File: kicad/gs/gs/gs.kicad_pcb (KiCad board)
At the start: 2 copper layers, 200 x 223.2 mm, 49 parts, among them J1 Jack_12V, J2 JST_MotorAz, J3 JST_MotorEl, J5 Breakout_DIP, J6 JST_ZeroAZ, U1 ESP32-WROOM-32-DEV, U2 MPU-9250-DEV, U3 Ai-Thinker-Ra-02, U4 L7805, U5 LD1117S33TR_SOT223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

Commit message: Finished second revision of GS PCB
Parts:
- added J4: Conn_02x10_Odd_Even, Connector_PinHeader_2.54mm:PinHeader_2x10_P2.54mm_Vertical, F.Cu at (214.1, 171.4)
- added JP1: PowerSelect_3V3, Connector_PinHeader_2.54mm:PinHeader_1x02_P2.54mm_Vertical, F.Cu at (265.7, 152.1)
- added JP2: PowerSelect_5V, Connector_PinHeader_2.54mm:PinHeader_1x02_P2.54mm_Vertical, F.Cu at (264.7, 114.0)
- added JP3: PowerSelect_24V, Connector_PinHeader_2.54mm:PinHeader_1x02_P2.54mm_Vertical, F.Cu at (149.9, 107.4)
- J5: value Breakout_DIP -> PowerBreakout; footprint Connector_PinSocket_2.54mm:PinSocket_1x10_P2.54mm_Vertical -> Connector_PinHeader_2.54mm:PinHeader_1x05_P2.54mm_Vertical
- U3: footprint RF_Module:Ai-Thinker-Ra-01-LoRa -> RA-02-PCB:RA-02-PCB
- moved J6 135.9 mm to (230.1, 222.8), turned to 180 degrees
- moved J3 101.8 mm to (197.6, 103.0)
- moved J5 97.9 mm to (237.2, 107.2), turned to 90 degrees
- moved J2 93.4 mm to (192.0, 97.0), turned to -90 degrees
- moved U9 54.4 mm to (108.0, 143.5), turned to 90 degrees
- moved U2 41.7 mm to (206.6, 167.3), turned to -90 degrees
- moved C6 24.9 mm to (259.5, 196.6), turned to 180 degrees
- moved C2 20.8 mm to (266.2, 110.3), turned to 90 degrees
- moved C21 17.9 mm to (130.5, 147.3)
- moved C4 17.7 mm to (271.8, 141.0), turned to 180 degrees
- moved C5 15.7 mm to (260.9, 191.5), turned to 0 degrees
- moved U5 13.5 mm to (275.3, 145.0), turned to 180 degrees
- moved R10 13.4 mm to (206.2, 64.3), turned to -90 degrees
- moved U4 13.0 mm to (274.8, 117.3), turned to 180 degrees
- moved C19 11.8 mm to (202.4, 66.5), turned to 90 degrees
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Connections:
- net Net-(J2-Pin_1) renamed M1_1A
- net Net-(J2-Pin_2) renamed M1_1B
- net Net-(J2-Pin_3) renamed M1_2A
- net Net-(J2-Pin_4) renamed M1_2B
- net Net-(J3-Pin_1) renamed M2_1A
- net Net-(J3-Pin_2) renamed M2_1B
- net Net-(J3-Pin_3) renamed M2_2A
- net Net-(J3-Pin_4) renamed M2_2B
- C2 pad 1: +5V -> 5V_Int
- C3 pad 1: +3V3 -> 3V3_Int
- J1 pad 3: unconnected-(J1-Pad3) -> GND
- J5 pad 1: BRK_TX -> GND
- J5 pad 2: BRK_RX -> GND
- J5 pad 3: BRK_VP -> +24V
- J5 pad 4: BRK_VN -> +5V
- J5 pad 5: BRK_GPIO25 -> +3V3
- U1 pad 10: AZ_ZERO -> M2_P1
- U1 pad 11: M1_I11 -> M2_I11
- U1 pad 12: M1_I12 -> M2_P2
- U1 pad 13: M1_P2 -> M2_I12
- U1 pad 18: BRK_TX -> M1_I01
- U1 pad 19: BRK_RX -> M1_I02
- U1 pad 2: BRK_VP -> AZ_ZERO
- U1 pad 23: RF_NRESET -> BRK_GPIO5
- U1 pad 26: RF_DIO2 -> BRK_GPIO4
- U1 pad 27: RF_DIO1 -> BRK_GPIO2
- U1 pad 3: BRK_VN -> IMU_INT
- U1 pad 4: IMU_INT -> M1_P1
- U1 pad 5: M1_I01 -> M1_I11
- U1 pad 6: M1_I02 -> M1_I12
- U1 pad 7: M1_P1 -> M1_P2
- U1 pad 8: BRK_GPIO25 -> M2_I01
- U1 pad 9: BRK_GPIO26 -> M2_I02
- U3 pad 10: RF_DIO4 -> RF_NSS
- U3 pad 11: RF_DIO5 -> SPI_MOSI
- U3 pad 12: SPI_SCK -> SPI_MISO
- U3 pad 13: SPI_MISO -> SPI_SCK
- U3 pad 14: SPI_MOSI -> RF_DIO5
- U3 pad 15: RF_NSS -> RF_DIO4
- U4 pad 3: +5V -> 5V_Int
- U5 pad 2: +3V3 -> 3V3_Int
- U7 pad 3: +24V -> 24V_Int
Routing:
- net +5V: track 0.00 -> 400.0 mm, vias 0 -> 1
- net +3V3: track 0.00 -> 280.2 mm
- net M1_I11: track 0.00 -> 271.5 mm, vias 0 -> 2
- net M1_I12: track 0.00 -> 260.3 mm, vias 0 -> 1
- net M1_P1: track 0.00 -> 257.1 mm, vias 0 -> 1
- net M1_P2: track 0.00 -> 257.0 mm, vias 0 -> 1
- net M1_I02: track 0.00 -> 222.4 mm, vias 0 -> 2
- net M1_I01: track 0.00 -> 216.8 mm, vias 0 -> 2
- net M2_I02: track 0.00 -> 212.8 mm, vias 0 -> 2
- net SPI_MOSI: track 0.00 -> 210.4 mm, vias 0 -> 1
- net M2_I12: track 0.00 -> 205.7 mm, vias 0 -> 2
- net M2_P2: track 0.00 -> 205.4 mm, vias 0 -> 2
- net M2_I01: track 0.00 -> 192.3 mm, vias 0 -> 2
- net M2_I11: track 0.00 -> 187.6 mm, vias 0 -> 2
- net M2_P1: track 0.00 -> 184.0 mm, vias 0 -> 2
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- added copper zone on B.Cu, net GND
- added copper zone on F.Cu, net GND
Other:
- board size 200 x 223.2 mm -> 198 x 198 mm
- board text added: "+24V"
- board text added: "+24V frm conv"
- board text added: "+24V to PCB"
- board text added: "+3V3"
- board text added: "+3V3 frm reg"
- board text added: "+3V3 to PCB"
- board text added: "+5V"
- board text added: "+5V frm reg"
- board text added: "+5V to PCB"
- board text added: "GND"
- board text added: "GPIO4"
- board text added: "GPIO5"
- board text added: "MotorAz"
- board text added: "MotorEl"
- board text added: "RF_DIO1"
- board text added: "RF_DIO2"
- board text added: "RF_DIO3"
- board text added: "RF_DIO4"
- board text added: "RF_DIO5"
- board text added: "RF_NRESET"
- board text added: "Zero Sensor"

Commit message: 2nd design of GS PCB
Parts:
- added R15: 10k, Resistor_THT:R_Axial_DIN0207_L6.3mm_D2.5mm_P10.16mm_Horizontal, F.Cu at (295.5, 173.0)
- C14, C15: value 820pF -> 100nF; footprint Capacitor_THT:C_Rect_L4.6mm_W2.0mm_P2.50mm_MKS02_FKP02 -> Capacitor_THT:C_Rect_L7.0mm_W4.5mm_P5.00mm
- C16: value 100nF -> 100uF; footprint Capacitor_THT:C_Rect_L7.0mm_W4.5mm_P5.00mm -> Capacitor_THT:CP_Radial_D5.0mm_P2.00mm
- C17: value 100nF -> 820pF; footprint Capacitor_THT:C_Rect_L7.0mm_W4.5mm_P5.00mm -> Capacitor_THT:C_Rect_L4.6mm_W2.0mm_P2.50mm_MKS02_FKP02
- C20: value 100uF -> 820pF; footprint Capacitor_THT:CP_Radial_D5.0mm_P2.00mm -> Capacitor_THT:C_Rect_L4.6mm_W2.0mm_P2.50mm_MKS02_FKP02
- R12: value 1k -> 1Ω
- R13: value 1Ω -> 1k
- moved R12 163.8 mm to (212.3, 230.1)
- moved C19 160.1 mm to (212.1, 226.3)
- moved C15 147.7 mm to (222.8, 219.8), turned to -90 degrees
- moved R10 146.4 mm to (196.7, 210.4), turned to 90 degrees
- moved C3 142.8 mm to (135.1, 115.1), turned to -135 degrees
- moved U5 142.0 mm to (137.3, 111.8), turned to -45 degrees
- moved C17 139.2 mm to (202.2, 223.8), turned to -90 degrees
- moved C4 134.7 mm to (138.9, 118.9), turned to -135 degrees
- moved U8 131.2 mm to (210.3, 209.8)
- moved R9 129.8 mm to (202.2, 219.7), turned to 0 degrees
- moved C16 127.7 mm to (222.6, 215.4), turned to 0 degrees
- moved C14 127.5 mm to (197.0, 214.4), turned to -90 degrees
- moved R14 125.0 mm to (216.4, 194.3), turned to 0 degrees
- moved R4 121.7 mm to (154.4, 194.0), turned to 90 degrees
- moved R11 119.4 mm to (217.2, 218.2), turned to -90 degrees
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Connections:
- net Net-(U6-SENSE1) renamed /M1_Sense1_In
- net Net-(U6-SENSE2) renamed /M1_Sense2_In
- C14 pad 1: Net-(U8-RC1) -> +5V
- C15 pad 1: GND -> +24V
- C15 pad 2: Net-(U8-RC2) -> GND
- C16 pad 1: +5V -> +24V
- C17 pad 1: +24V -> Net-(U8-RC1)
- C18 pad 2: Net-(U8-COMP_IN1) -> Net-(U8-RC2)
- C19 pad 2: Net-(U8-COMP_IN2) -> Net-(U8-COMP_IN1)
- C20 pad 1: +24V -> GND
- C20 pad 2: GND -> Net-(U8-COMP_IN2)
- C4 pad 1: +5V -> 5V_Int
- J2 pad 1: M1_1A -> M1_1B
- J2 pad 2: M1_1B -> M1_1A
- J2 pad 3: M1_2A -> M1_2B
- J2 pad 4: M1_2B -> M1_2A
- J3 pad 1: M2_1A -> M2_1B
- J3 pad 2: M2_1B -> M2_1A
- J3 pad 3: M2_2A -> M2_2B
- J3 pad 4: M2_2B -> M2_2A
- J4 pad 1: BRK_GPIO2 -> RF_DIO1
- J4 pad 10: RF_DIO3 -> SPI_MISO
- J4 pad 11: SPI_MISO -> unconnected-(J4-Pin_11-Pad11)
- J4 pad 12: RF_DIO2 -> SPI_SCK
- J4 pad 14: RF_DIO1 -> RF_DIO5
- J4 pad 16: RF_NRESET -> RF_DIO4
- J4 pad 18: RF_DIO4 -> unconnected-(J4-Pin_18-Pad18)
- J4 pad 2: unconnected-(J4-Pin_2-Pad2) -> BRK_GPIO14
- J4 pad 20: RF_DIO5 -> unconnected-(J4-Pin_20-Pad20)
- J4 pad 3: BRK_GPIO4 -> RF_DIO3
- J4 pad 4: unconnected-(J4-Pin_4-Pad4) -> BRK_GPIO12
- J4 pad 5: BRK_GPIO5 -> RF_DIO2
- J4 pad 6: unconnected-(J4-Pin_6-Pad6) -> BRK_GPIO13
- J4 pad 7: SPI_SCK -> RF_NRESET
- J4 pad 8: unconnected-(J4-Pin_8-Pad8) -> SPI_MOSI
- J4 pad 9: SPI_MOSI -> unconnected-(J4-Pin_9-Pad9)
- J5 pad 3: +24V -> GND
- R11 pad 1: Net-(U8-SENSE1) -> /M2_Sense1_In
- R12 pad 1: Net-(U8-SENSE2) -> /M2_Sense1_In
- R12 pad 2: Net-(U8-COMP_IN2) -> GND
- R13 pad 1: Net-(U8-SENSE1) -> /M2_Sense2_In
- R13 pad 2: GND -> Net-(U8-COMP_IN2)
- R14 pad 1: Net-(U8-SENSE2) -> /M2_Sense2_In
- U1 pad 1: +5V -> unconnected-(U1-EN-Pad1)
- U1 pad 10: M2_P1 -> RF_NSS
- U1 pad 11: M2_I11 -> BRK_GPIO14
- U1 pad 12: M2_P2 -> BRK_GPIO12
- U1 pad 13: M2_I12 -> BRK_GPIO13
- U1 pad 18: M1_I01 -> M2_I01
- U1 pad 19: M1_I02 -> M2_I11
- U1 pad 20: RF_NSS -> M2_P1
- U1 pad 23: BRK_GPIO5 -> M2_P2
- U1 pad 26: BRK_GPIO4 -> M2_I12
- U1 pad 27: BRK_GPIO2 -> M2_I02
- U1 pad 4: M1_P1 -> M1_I01
- U1 pad 6: M1_I12 -> M1_P1
- U1 pad 8: M2_I01 -> M1_I12
- U1 pad 9: M2_I02 -> M1_I02
- U5 pad 3: +5V -> 5V_Int
- U8 pad 23: Net-(U8-SENSE1) -> /M2_Sense1_In
- U8 pad 3: Net-(U8-SENSE2) -> /M2_Sense2_In
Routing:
- net +5V: track 400.0 -> 142.8 mm, vias 1 -> 0
- net M2_I02: track 212.8 -> 42.3 mm, vias 2 -> 0
- net M2_I12: track 205.7 -> 45.7 mm, vias 2 -> 0
- net M2_P2: track 205.4 -> 51.3 mm, vias 2 -> 0
- net M1_I11: track 271.5 -> 122.2 mm, vias 2 -> 0
- net 5V_Int: track 10.8 -> 159.3 mm
- net M1_I12: track 260.3 -> 118.2 mm, vias 1 -> 0
- net M2_I01: track 192.3 -> 50.6 mm, vias 2 -> 0
- net M2_I11: track 187.6 -> 53.0 mm, vias 2 -> 0
- net M1_P1: track 257.1 -> 122.5 mm, vias 1 -> 0
- net M1_P2: track 257.0 -> 122.7 mm, vias 1 -> 0
- net M2_P1: track 184.0 -> 54.1 mm, vias 2 -> 0
- net MREF: track 166.8 -> 46.4 mm, vias 2 -> 0
- net RF_NSS: track 154.4 -> 45.7 mm
- net M1_I02: track 222.4 -> 114.2 mm, vias 2 -> 0
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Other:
- outline, holes or cut-outs redrawn
- board text removed: "+24V"
- board text removed: "+24V frm conv"
- board text removed: "+24V to PCB"
- board text removed: "+3V3"
- board text removed: "+3V3 frm reg"
- board text removed: "+3V3 to PCB"
- board text removed: "+5V"
- board text removed: "+5V frm reg"
- board text removed: "+5V to PCB"
- board text removed: "GND"
- board text removed: "GPIO4"
- board text removed: "GPIO5"
- board text removed: "MotorAz"
- board text removed: "MotorEl"
- board text removed: "RF_DIO1"
- board text removed: "RF_DIO2"
- board text removed: "RF_DIO3"
- board text removed: "RF_DIO4"
- board text removed: "RF_DIO5"
- board text removed: "RF_NRESET"
- board text removed: "Zero Sensor"

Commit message: Finished core of 2nd design of GS PCB
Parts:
- moved R1 7.64 mm to (189.5, 168.4)
- moved R2 7.62 mm to (194.6, 168.4)
- moved C13 6.90 mm to (169.2, 177.0)
- moved U4 6.68 mm to (164.8, 81.1)
- moved C20 3.61 mm to (212.1, 195.1)
- moved R5 3.05 mm to (174.5, 200.2)
- moved C1 2.54 mm to (174.2, 75.4)
- moved R8 1.93 mm to (172.7, 175.8)
- moved R7 1.83 mm to (173.7, 180.3)
- moved C2 1.02 mm to (164.6, 75.4)
- moved J4 0.51 mm to (295.4, 145.3)
- turned C17 to 0 degrees
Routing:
- net +5V: track 142.8 -> 243.2 mm, vias 0 -> 1
- net MREF: track 46.4 -> 142.4 mm, vias 0 -> 2
- net AZ_ZERO: track 0.00 -> 62.6 mm, vias 0 -> 1
- net Net-(U6-COMP_IN2): track 0.00 -> 21.5 mm
- net IMU_INT: track 100.3 -> 115.9 mm, vias 0 -> 1
- net /M1_Sense2_In: track 0.00 -> 15.1 mm
- net RF_NSS: track 45.7 -> 60.7 mm
- net Net-(U6-RC2): track 0.00 -> 13.1 mm
- net RF_DIO0: track 68.8 -> 81.2 mm
- net +12V: track 114.9 -> 121.5 mm
- net Net-(U8-COMP_IN2): track 12.8 -> 18.1 mm
- net /M1_Sense1_In: track 27.9 -> 22.7 mm
- net GND: track 0.00 -> 5.08 mm
- net 5V_Int: track 159.3 -> 154.2 mm
- net 3V3_Int: track 86.8 -> 91.4 mm
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
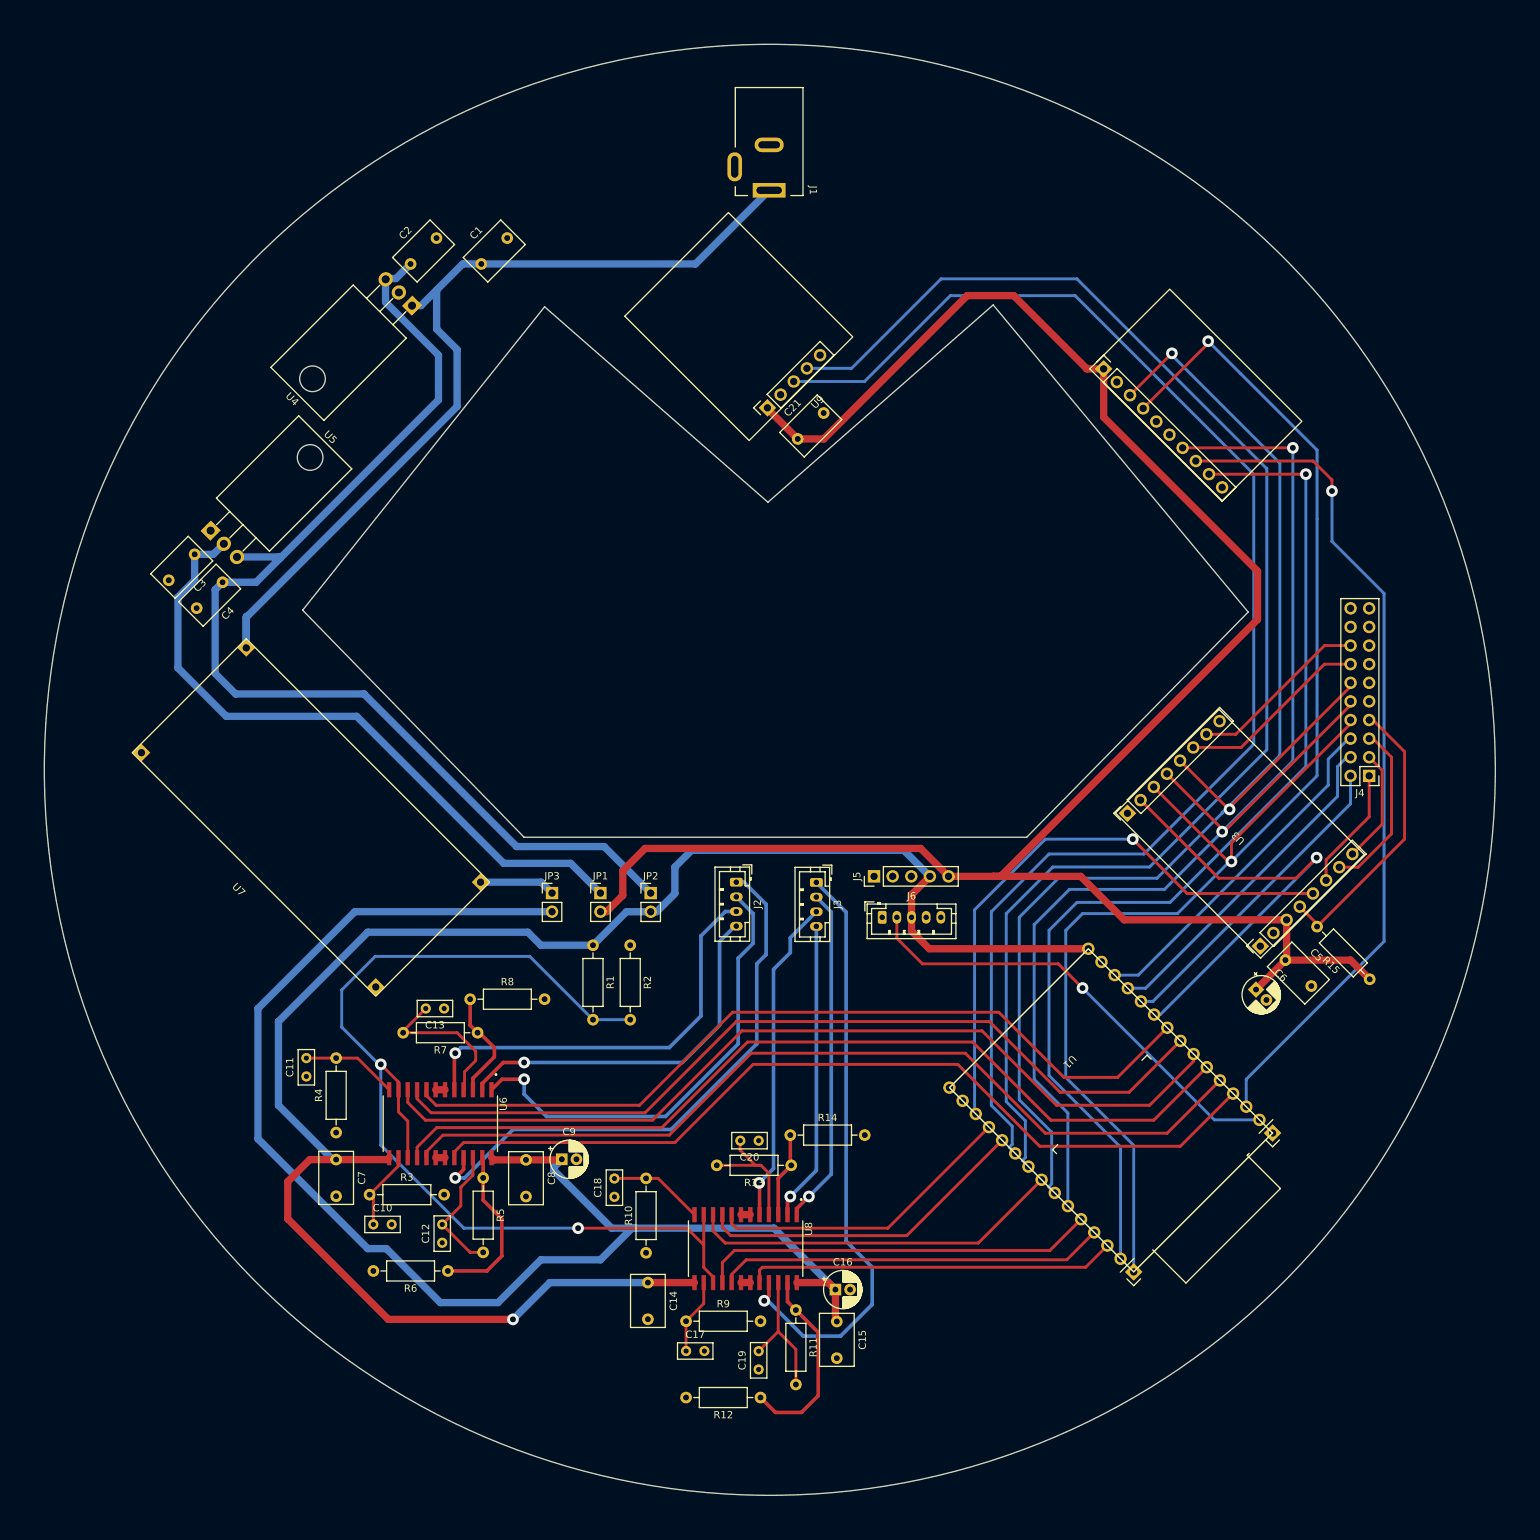
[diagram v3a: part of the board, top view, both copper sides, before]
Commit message: Added details to GS PCB
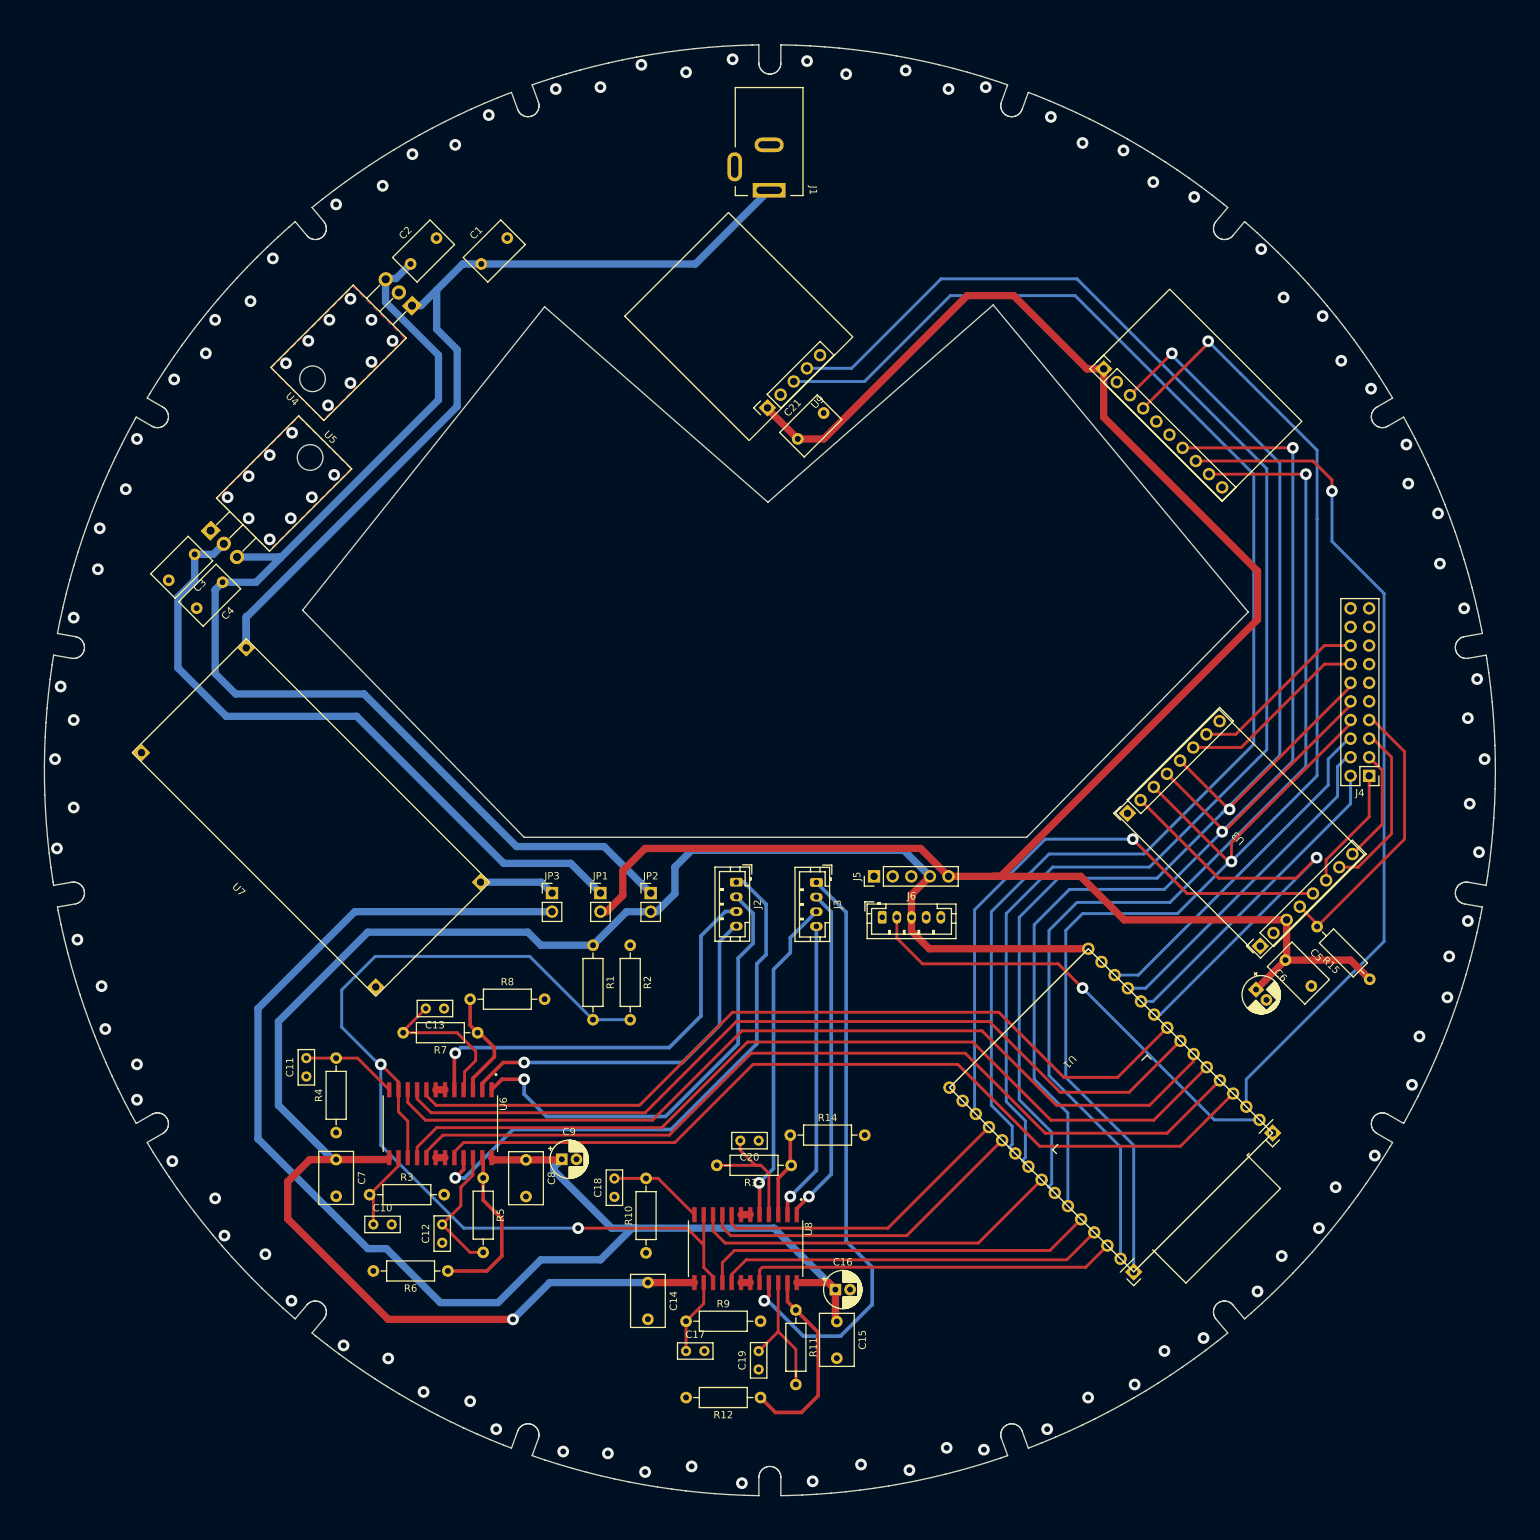
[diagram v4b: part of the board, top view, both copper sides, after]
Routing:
- net Heatsink5V: vias 0 -> 9
- net Heatsink3V3: vias 0 -> 9
- net GND: vias 0 -> 90
- added copper zone on F.Cu, net Heatsink3V3
- added copper zone on F.Cu, net Heatsink5V
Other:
- outline, holes or cut-outs redrawn

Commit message: Finished GS PCB Rev 4
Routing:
- net Heatsink5V: vias 9 -> 0
- net Heatsink3V3: vias 9 -> 0
- net (no net): vias 0 -> 18
- added copper zone on F.Cu, net (none)
- removed copper zone on F.Cu, net Heatsink3V3
- removed copper zone on F.Cu, net Heatsink5V
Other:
- board text added: "+24V (from)"
- board text added: "+24V (to)"
- board text added: "+3V3"
- board text added: "+3V3 (from)"
- board text added: "+3V3 (to)"
- board text added: "+5V"
- board text added: "+5V (from)"
- board text added: "+5V (to)"
- board text added: "GND"
